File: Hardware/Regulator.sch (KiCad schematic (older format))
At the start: 13 parts, among them U2 MIC5209-3.3, U3 LT1376IS8-5

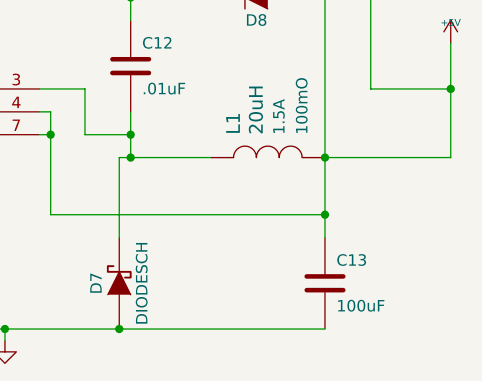
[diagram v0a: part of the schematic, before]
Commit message: Switched to tantalum capacitor for power supply
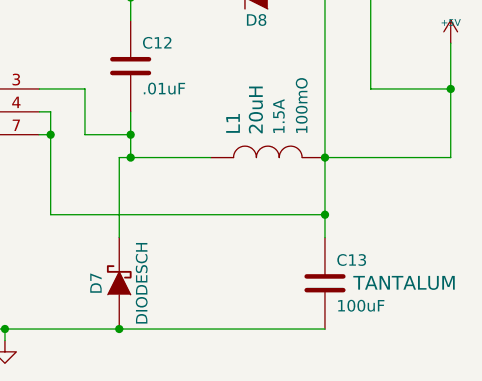
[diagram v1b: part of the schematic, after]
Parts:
- C13: footprint Local:SMD_CAP -> Capacitors_Tantalum_SMD:TantalC_SizeD_EIA-7343_HandSoldering; Field4 (none) -> TANTALUM
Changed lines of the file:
@@
 LIBS:STM32-Additional
 LIBS:xbee
+LIBS:Passives
 LIBS:avbay-cache
 EELAYER 25 0
@@
 $EndDescr
 $Comp
-L 3V3 #PWR019
+L 3V3 #PWR18
 U 1 1 543769E5
 P 2300 2050
-F 0 "#PWR019" H 2300 2150 40  0001 C CNN
+F 0 "#PWR18" H 2300 2150 40  0001 C CNN
 F 1 "3V3" H 2300 2175 40  0000 C CNN
 F 2 "" H 2300 2050 60  0000 C CNN
@@
 Vbatt
 $Comp
-L GND #PWR020
+L GND #PWR16
 U 1 1 54376AC4
 P 1650 2650
-F 0 "#PWR020" H 1650 2650 30  0001 C CNN
+F 0 "#PWR16" H 1650 2650 30  0001 C CNN
 F 1 "GND" H 1650 2580 30  0001 C CNN
 F 2 "" H 1650 2650 60  0000 C CNN
@@
 $EndComp
 $Comp
-L +5V #PWR021
+L +5V #PWR19
 U 1 1 544485F5
 P 4050 3300
-F 0 "#PWR021" H 4050 3390 20  0001 C CNN
+F 0 "#PWR19" H 4050 3390 20  0001 C CNN
 F 1 "+5V" H 4050 3390 30  0000 C CNN
 F 2 "" H 4050 3300 60  0000 C CNN
@@
 $EndComp
 $Comp
-L GND #PWR022
+L GND #PWR17
 U 1 1 55058B68
 P 2100 4600
-F 0 "#PWR022" H 2100 4600 30  0001 C CNN
+F 0 "#PWR17" H 2100 4600 30  0001 C CNN
 F 1 "GND" H 2100 4530 30  0001 C CNN
 F 2 "" H 2100 4600 60  0000 C CNN
@@
 F 0 "C13" H 3550 4450 50  0000 L CNN
 F 1 "100uF" H 3550 4250 50  0000 L CNN
-F 2 "Local:SMD_CAP" H 3538 4200 30  0001 C CNN
+F 2 "Capacitors_Tantalum_SMD:TantalC_SizeD_EIA-7343_HandSoldering" H 3538 4200 30  0001 C CNN
 F 3 "" H 3500 4350 60  0000 C CNN
+F 4 "TANTALUM" H 3850 4350 60  0000 C CNN "Field4"
 	1    3500 4350
 	1    0    0    -1
